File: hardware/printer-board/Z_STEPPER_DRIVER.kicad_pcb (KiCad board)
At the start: 2 copper layers, 7 parts, among them J7 MS_SELECT, J8 TO_MOTOR, U5 A4988_MODULE

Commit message: update heater layouts,
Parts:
- removed C11: CP100uf,25V, Capacitor_SMD:CP_Elec_6.3x7.7
- removed R9: R103,0603, Resistor_SMD:R_0603_1608Metric_Pad1.05x0.95mm_HandSolder
- added C9: C104,0603, Capacitor_SMD:C_0603_1608Metric_Pad1.05x0.95mm_HandSolder, F.Cu at (38.0, 31.5)
- added D22: LED_BLUE,0603, LED_SMD:LED_0603_1608Metric_Pad1.05x0.95mm_HandSolder, F.Cu at (43.5, 53.0)
- added R15: R102,0603, Resistor_SMD:R_0603_1608Metric_Pad1.05x0.95mm_HandSolder, B.Cu at (43.5, 53.0)
- added R19: R103,0603, Resistor_SMD:R_0603_1608Metric_Pad1.05x0.95mm_HandSolder, F.Cu at (41.5, 33.5)
- J8: value TO_MOTOR -> Z
- moved J8 22.4 mm to (32.5, 53.0), turned to 90 degrees
- moved R8 10.1 mm to (41.5, 37.5)
- moved J7 1.58 mm to (35.5, 35.5)
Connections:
- net +5V renamed +3V3_STM32
- net /DIR renamed /Z_DIR
- net /STEP renamed /Z_STEP
- U5 pad 1: /~EN~ -> /~Z_EN~
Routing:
- net +3V3_STM32: track 33.6 -> 0.00 mm
- net GND: track 31.9 -> 0.00 mm
- net +12V: track 19.8 -> 0.00 mm
- net Net-(J7-Pad1): track 16.6 -> 0.00 mm
- net Net-(J7-Pad5): track 5.82 -> 0.00 mm
- net Net-(J7-Pad3): track 5.82 -> 0.00 mm
- net Net-(J8-Pad4): track 3.41 -> 0.00 mm
- net Net-(J8-Pad3): track 3.41 -> 0.00 mm
- net Net-(J8-Pad2): track 3.41 -> 0.00 mm
- net Net-(J8-Pad1): track 3.41 -> 0.00 mm
- net /~EN~: track 3.40 -> 0.00 mm
- net Net-(U5-Pad5): track 2.54 -> 0.00 mm

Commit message: update,
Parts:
- J8: footprint Connector_PinHeader_2.54mm:PinHeader_1x04_P2.54mm_Vertical -> footprint-lib:b4b-ph-kl,stepper_terminal
- U5: footprint Module:Pololu_Breakout-16_15.2x20.3mm -> footprint-lib:Pololu_Breakout-16_15.2x20.3mm
- moved J8 3.71 mm to (36.2, 53.2), turned to 0 degrees

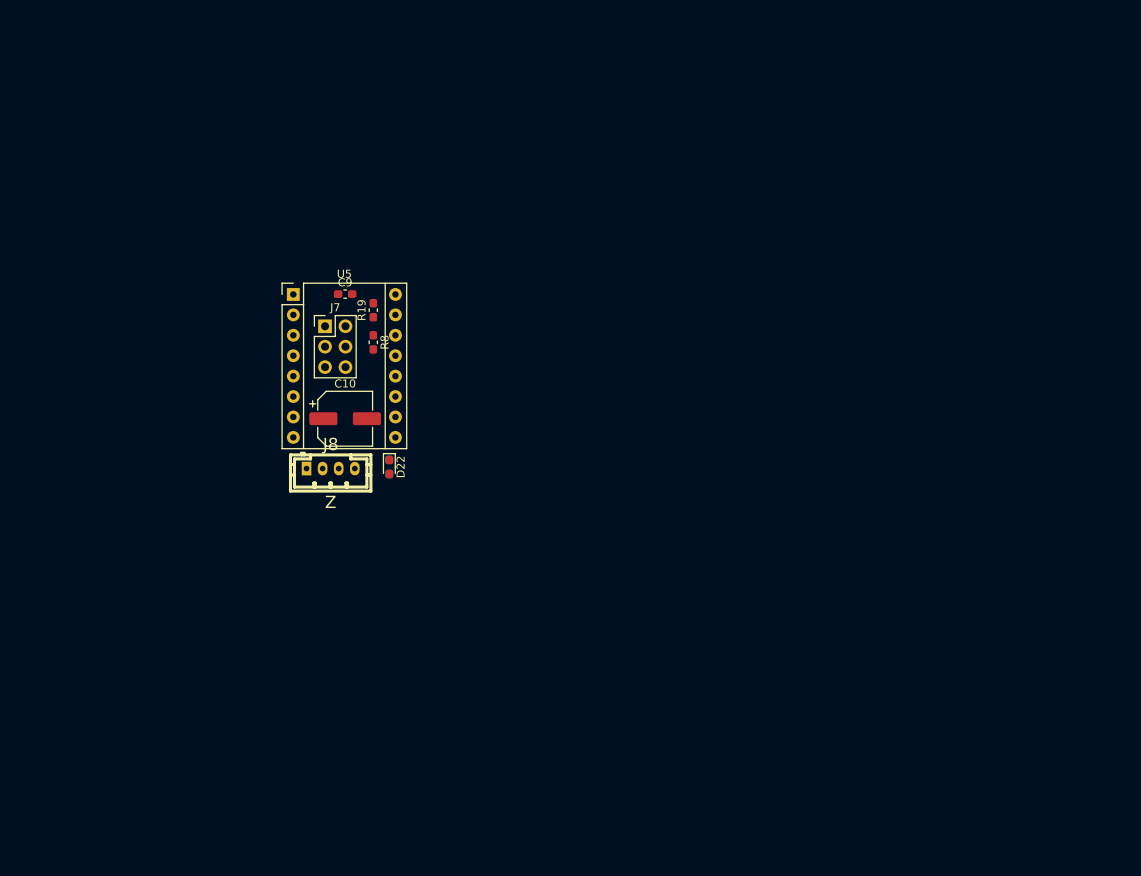
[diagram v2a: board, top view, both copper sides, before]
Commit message: update for stepper Z,
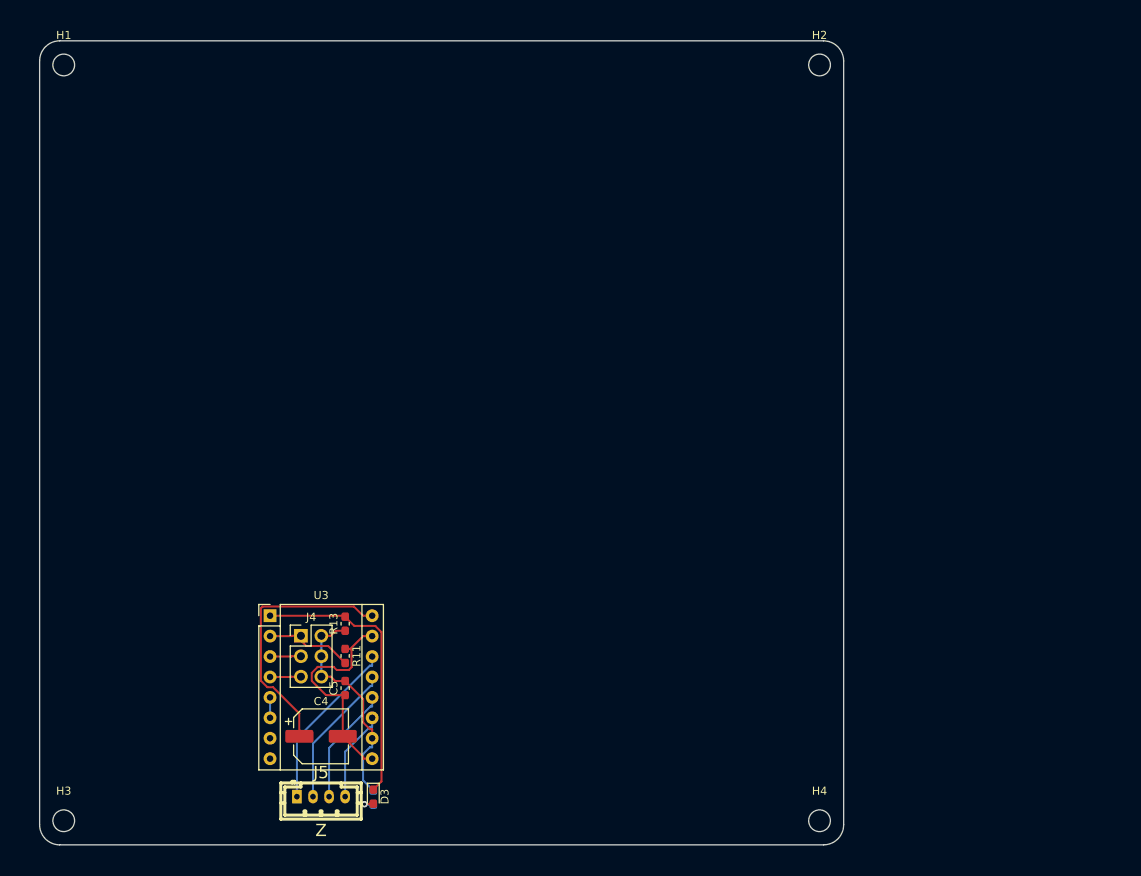
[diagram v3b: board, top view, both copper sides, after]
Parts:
- removed C10: CP100uf,25V, Capacitor_SMD:CP_Elec_6.3x7.7
- removed C9: C104,0603, Capacitor_SMD:C_0603_1608Metric_Pad1.05x0.95mm_HandSolder
- removed D22: LED_BLUE,0603, LED_SMD:LED_0603_1608Metric_Pad1.05x0.95mm_HandSolder
- removed J7: MS_SELECT, Connector_PinHeader_2.54mm:PinHeader_2x03_P2.54mm_Vertical
- removed J8: Z, footprint-lib:b4b-ph-kl,stepper_terminal
- removed R15: R102,0603, Resistor_SMD:R_0603_1608Metric_Pad1.05x0.95mm_HandSolder
- removed R19: R103,0603, Resistor_SMD:R_0603_1608Metric_Pad1.05x0.95mm_HandSolder
- removed R8: R104,0603, Resistor_SMD:R_0603_1608Metric_Pad1.05x0.95mm_HandSolder
- removed U5: A4988_MODULE, footprint-lib:Pololu_Breakout-16_15.2x20.3mm
- added C4: CP100uf,25V, Capacitor_SMD:CP_Elec_6.3x7.7, F.Cu at (35.0, 86.5)
- added C5: C104,0603, Capacitor_SMD:C_0603_1608Metric_Pad1.05x0.95mm_HandSolder, F.Cu at (38.0, 80.5)
- added D3: LED_BLUE,0603, LED_SMD:LED_0603_1608Metric_Pad1.05x0.95mm_HandSolder, F.Cu at (41.5, 94.0)
- added H1: MOUNT_M3, MountingHole:MountingHole_2.7mm_M2.5, F.Cu at (3.00, 3.00)
- added H2: MOUNT_M3, MountingHole:MountingHole_2.7mm_M2.5, F.Cu at (97.0, 3.00)
- added H3: MOUNT_M3, MountingHole:MountingHole_2.7mm_M2.5, F.Cu at (3.00, 97.0)
- added H4: MOUNT_M3, MountingHole:MountingHole_2.7mm_M2.5, F.Cu at (97.0, 97.0)
- added J4: MS_SELECT, Connector_PinHeader_2.54mm:PinHeader_2x03_P2.54mm_Vertical, F.Cu at (32.5, 74.0)
- added J5: Z, footprint-lib:b4b-ph-kl,stepper_terminal, F.Cu at (35.0, 94.0)
- added R11: R104,0603, Resistor_SMD:R_0603_1608Metric_Pad1.05x0.95mm_HandSolder, F.Cu at (38.0, 76.5)
- added R12: R102,0603, Resistor_SMD:R_0603_1608Metric_Pad1.05x0.95mm_HandSolder, B.Cu at (41.5, 94.1)
- added R13: R103,0603, Resistor_SMD:R_0603_1608Metric_Pad1.05x0.95mm_HandSolder, F.Cu at (38.0, 72.5)
- added U3: A4988_MODULE, footprint-lib:Pololu_Breakout-16_15.2x20.3mm, F.Cu at (28.7, 71.5)
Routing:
- net /Z_~E1_STEP~PER_DRIVER/~Z_EN~: track 0.00 -> 34.7 mm
- net +12V: track 0.00 -> 32.7 mm
- net GND: track 0.00 -> 27.9 mm
- net +3V3: track 0.00 -> 27.8 mm
- net Net-(J5-Pad1): track 0.00 -> 21.5 mm
- net Net-(J5-Pad2): track 0.00 -> 18.0 mm
- net Net-(J5-Pad3): track 0.00 -> 14.7 mm
- net Net-(J5-Pad4): track 0.00 -> 11.4 mm
- net Net-(J4-Pad1): track 0.00 -> 11.3 mm
- net Net-(J4-Pad5): track 0.00 -> 3.86 mm
- net Net-(J4-Pad3): track 0.00 -> 3.86 mm
- net Net-(U3-Pad5): track 0.00 -> 2.54 mm
- net Net-(D3-Pad2): track 0.00 -> 2.25 mm, vias 0 -> 1
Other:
- board outline added: 100 x 100 mm

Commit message: update,
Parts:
- removed H1, H2, H3, H4: MOUNT_M3, MountingHole:MountingHole_2.7mm_M2.5
- moved C4 73.1 mm to (9.50, 18.0)
- moved C5 73.1 mm to (12.5, 12.0)
- moved D3 73.1 mm to (16.0, 25.5)
- moved J4 73.1 mm to (7.00, 5.50)
- moved J5 73.1 mm to (9.50, 25.5)
- moved R11 73.1 mm to (12.5, 8.00)
- moved R12 73.1 mm to (16.0, 25.6)
- moved R13 73.1 mm to (12.5, 4.00)
- moved U3 73.1 mm to (3.16, 3.00)
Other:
- board outline removed

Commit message: update,
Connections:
- net +3V3 renamed +3V3_STM32
- net /Z_~E1_STEP~PER_DRIVER/Z_DIR renamed /Z_DIR
- net /Z_~E1_STEP~PER_DRIVER/Z_STEP renamed /Z_STEP
- net /Z_~E1_STEP~PER_DRIVER/~Z_EN~ renamed /~Z_EN~

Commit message: update,
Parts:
- added C1: CP100uf,10V, Capacitor_SMD:CP_Elec_6.3x5.3, F.Cu at (76.3, 33.4)
- added C10: CP100uf,25V, Capacitor_SMD:CP_Elec_6.3x7.7, F.Cu at (9.23, 64.2)
- added C11: C104,0603, Capacitor_SMD:C_0603_1608Metric_Pad1.05x0.95mm_HandSolder, F.Cu at (20.6, 67.2)
- added C12: CP100uf,25V, Capacitor_SMD:CP_Elec_6.3x7.7, F.Cu at (9.23, 48.3)
- added C13: C104,0603, Capacitor_SMD:C_0603_1608Metric_Pad1.05x0.95mm_HandSolder, F.Cu at (16.8, 51.3)
- added C14: C106,0603, Capacitor_SMD:C_0603_1608Metric_Pad1.05x0.95mm_HandSolder, B.Cu at (2.75, 31.8)
- added C15: C106,0603, Capacitor_SMD:C_0603_1608Metric_Pad1.05x0.95mm_HandSolder, B.Cu at (10.0, 31.8)
- added C16: C106,0603, Capacitor_SMD:C_0603_1608Metric_Pad1.05x0.95mm_HandSolder, B.Cu at (16.8, 31.8)
- added C17: C106,0603, Capacitor_SMD:C_0603_1608Metric_Pad1.05x0.95mm_HandSolder, B.Cu at (23.5, 31.8)
- added C18: C106,0603, Capacitor_SMD:C_0603_1608Metric_Pad1.05x0.95mm_HandSolder, B.Cu at (27.4, 20.1)
- added C19: C104,0603, Capacitor_SMD:C_0603_1608Metric_Pad1.05x0.95mm_HandSolder, F.Cu at (11.0, 1.75)
- added C2: CP100uf,25V, Capacitor_SMD:CP_Elec_6.3x7.7, F.Cu at (90.5, 90.2)
- added C20: CP100uf,35V, Capacitor_SMD:CP_Elec_6.3x7.7, F.Cu at (11.8, 9.35)
- added C21: C104,0603, Capacitor_SMD:C_0603_1608Metric_Pad1.05x0.95mm_HandSolder, B.Cu at (40.2, 69.8)
- added C22: C10pf,0603, Capacitor_SMD:C_0603_1608Metric_Pad1.05x0.95mm_HandSolder, B.Cu at (28.5, 62.2)
- added C23: C104,0603, Capacitor_SMD:C_0603_1608Metric_Pad1.05x0.95mm_HandSolder, B.Cu at (33.1, 60.3)
- added C24: C10pf,0603, Capacitor_SMD:C_0603_1608Metric_Pad1.05x0.95mm_HandSolder, B.Cu at (35.8, 69.2)
- added C25: C104,0603, Capacitor_SMD:C_0603_1608Metric_Pad1.05x0.95mm_HandSolder, B.Cu at (31.4, 56.1)
- added C26: C104,0603, Capacitor_SMD:C_0603_1608Metric_Pad1.05x0.95mm_HandSolder, B.Cu at (42.3, 47.9)
- added C27: C104,0603, Capacitor_SMD:C_0603_1608Metric_Pad1.05x0.95mm_HandSolder, B.Cu at (50.8, 58.5)
- added C28: C104,0603, Capacitor_SMD:C_0603_1608Metric_Pad1.05x0.95mm_HandSolder, B.Cu at (42.6, 66.6)
- added C29: C105,0603, Capacitor_SMD:C_0603_1608Metric_Pad1.05x0.95mm_HandSolder, B.Cu at (34.7, 61.9)
- added C3: C104,0603, Capacitor_SMD:C_0603_1608Metric_Pad1.05x0.95mm_HandSolder, F.Cu at (93.5, 74.8)
- added C30: C104,0603, Capacitor_SMD:C_0603_1608Metric_Pad1.05x0.95mm_HandSolder, B.Cu at (49.7, 59.6)
- added C31: C104,0603, Capacitor_SMD:C_0603_1608Metric_Pad1.05x0.95mm_HandSolder, B.Cu at (43.3, 49.0)
- added C32: C104,0603, Capacitor_SMD:C_0603_1608Metric_Pad1.05x0.95mm_HandSolder, B.Cu at (47.6, 68.0)
- added C36: CP1uf,50V, Capacitor_SMD:CP_Elec_4x5.3, F.Cu at (21.5, 13.8)
- added C37: CP1uf,50V, Capacitor_SMD:CP_Elec_4x5.3, F.Cu at (29.5, 13.8)
- added C38: CP1uf,50V, Capacitor_SMD:CP_Elec_4x5.3, F.Cu at (38.0, 13.8)
- added C39: CP100uf,25V, Capacitor_SMD:CP_Elec_6.3x7.7, F.Cu at (25.7, 90.2)
- added C40: C104,0603, Capacitor_SMD:C_0603_1608Metric_Pad1.05x0.95mm_HandSolder, F.Cu at (29.8, 78.6)
- added C41: CP100uf,25V, Capacitor_SMD:CP_Elec_6.3x7.7, F.Cu at (74.3, 90.2)
- added C42: C104,0603, Capacitor_SMD:C_0603_1608Metric_Pad1.05x0.95mm_HandSolder, F.Cu at (77.8, 74.8)
- added C43: C104,0603, Capacitor_SMD:C_0603_1608Metric_Pad1.05x0.95mm_HandSolder, F.Cu at (133.3, 61.4)
- added C44: CP100uf,16V, Capacitor_SMD:CP_Elec_6.3x5.3, F.Cu at (37.2, 21.0)
- added C45: C106,0603, Capacitor_SMD:C_0603_1608Metric_Pad1.05x0.95mm_HandSolder, F.Cu at (67.5, 33.5)
- added C46: C104,0603, Capacitor_SMD:C_0603_1608Metric_Pad1.05x0.95mm_HandSolder, F.Cu at (71.5, 40.0)
- added C47: C332,0603, Capacitor_SMD:C_0603_1608Metric_Pad1.05x0.95mm_HandSolder, F.Cu at (63.0, 41.0)
- added C48: C103,0603, Capacitor_SMD:C_0603_1608Metric_Pad1.05x0.95mm_HandSolder, F.Cu at (70.0, 32.5)
- added C49: C226,6.3v,0603, Capacitor_SMD:C_0603_1608Metric_Pad1.05x0.95mm_HandSolder, F.Cu at (63.0, 37.5)
- added C50: C106,0603, Capacitor_SMD:C_0603_1608Metric_Pad1.05x0.95mm_HandSolder, F.Cu at (48.2, 40.2)
- added C51: C104,0603, Capacitor_SMD:C_0603_1608Metric_Pad1.05x0.95mm_HandSolder, F.Cu at (43.5, 33.2)
- added C52: C332,0603, Capacitor_SMD:C_0603_1608Metric_Pad1.05x0.95mm_HandSolder, F.Cu at (49.2, 30.0)
- added C53: C103,0603, Capacitor_SMD:C_0603_1608Metric_Pad1.05x0.95mm_HandSolder, F.Cu at (45.5, 40.8)
- added C54: C226,6.3v,0603, Capacitor_SMD:C_0603_1608Metric_Pad1.05x0.95mm_HandSolder, F.Cu at (52.3, 35.5)
- added C55: C105,0603, Capacitor_SMD:C_0603_1608Metric_Pad1.05x0.95mm_HandSolder, B.Cu at (38.7, 65.9)
- added C6: CP100uf,25V, Capacitor_SMD:CP_Elec_6.3x7.7, F.Cu at (41.9, 90.2)
- added C7: C104,0603, Capacitor_SMD:C_0603_1608Metric_Pad1.05x0.95mm_HandSolder, F.Cu at (45.8, 78.6)
- added C8: CP100uf,25V, Capacitor_SMD:CP_Elec_6.3x7.7, F.Cu at (9.50, 90.2)
- added C9: C104,0603, Capacitor_SMD:C_0603_1608Metric_Pad1.05x0.95mm_HandSolder, F.Cu at (12.5, 82.5)
- added D1: 5V HEALTHY, LED_SMD:LED_0603_1608Metric_Pad1.05x0.95mm_HandSolder, F.Cu at (50.8, 70.8)
- added D10: LED_BLUE,0603, LED_SMD:LED_0603_1608Metric_Pad1.05x0.95mm_HandSolder, F.Cu at (91.9, 9.25)
- added D11: LED_BLUE,0603, LED_SMD:LED_0603_1608Metric_Pad1.05x0.95mm_HandSolder, F.Cu at (93.7, 9.30)
- added D12: LED_BLUE,0603, LED_SMD:LED_0603_1608Metric_Pad1.05x0.95mm_HandSolder, F.Cu at (95.4, 9.30)
- added D13: LED_BLUE,0603, LED_SMD:LED_0603_1608Metric_Pad1.05x0.95mm_HandSolder, F.Cu at (98.9, 9.30)
- added D14: LED_BLUE,0603, LED_SMD:LED_0603_1608Metric_Pad1.05x0.95mm_HandSolder, F.Cu at (97.2, 9.30)
- added D15: SD_M4, Diode_SMD:D_SOD-323_HandSoldering, F.Cu at (11.2, 3.75)
- added D16: SD_M4, Diode_SMD:D_SOD-323_HandSoldering, F.Cu at (21.4, 21.4)
- added D17: PB9, LED_SMD:LED_0603_1608Metric_Pad1.05x0.95mm_HandSolder, F.Cu at (30.3, 52.5)
- added D18: LED_RED,0603, LED_SMD:LED_0603_1608Metric_Pad1.05x0.95mm_HandSolder, F.Cu at (63.9, 5.50)
- added D19: LED_RED,0603, LED_SMD:LED_0603_1608Metric_Pad1.05x0.95mm_HandSolder, F.Cu at (75.8, 5.50)
- added D2: LED_BLUE,0603, LED_SMD:LED_0603_1608Metric_Pad1.05x0.95mm_HandSolder, F.Cu at (92.2, 97.7)
- added D20: LED_BLUE,0603, LED_SMD:LED_0603_1608Metric_Pad1.05x0.95mm_HandSolder, F.Cu at (25.1, 2.52)
- added D21: LED_BLUE,0603, LED_SMD:LED_0603_1608Metric_Pad1.05x0.95mm_HandSolder, F.Cu at (33.4, 2.52)
- added D22: LED_BLUE,0603, LED_SMD:LED_0603_1608Metric_Pad1.05x0.95mm_HandSolder, F.Cu at (41.8, 2.50)
- added D23: LED_BLUE,0603, LED_SMD:LED_0603_1608Metric_Pad1.05x0.95mm_HandSolder, F.Cu at (33.0, 97.7)
- added D24: LED_BLUE,0603, LED_SMD:LED_0603_1608Metric_Pad1.05x0.95mm_HandSolder, F.Cu at (78.2, 97.7)
- added D4: LED_BLUE,0603, LED_SMD:LED_0603_1608Metric_Pad1.05x0.95mm_HandSolder, F.Cu at (48.1, 97.7)
- added D5: LED_BLUE,0603, LED_SMD:LED_0603_1608Metric_Pad1.05x0.95mm_HandSolder, F.Cu at (17.8, 97.7)
- added D6: LED_BLUE,0603, LED_SMD:LED_0603_1608Metric_Pad1.05x0.95mm_HandSolder, F.Cu at (3.00, 70.5)
- added D7: LED_BLUE,0603, LED_SMD:LED_0603_1608Metric_Pad1.05x0.95mm_HandSolder, F.Cu at (3.00, 54.7)
- added D8: LED_RED,0603, LED_SMD:LED_0603_1608Metric_Pad1.05x0.95mm_HandSolder, F.Cu at (51.8, 5.50)
- added D9: LED_BLUE,0603, LED_SMD:LED_0603_1608Metric_Pad1.05x0.95mm_HandSolder, F.Cu at (90.2, 9.25)
- added F1: 16V/30A, w_misc_comp:fuse_smf, F.Cu at (11.8, 17.9)
- added F2: 30V/5A, w_misc_comp:fuse_smf, F.Cu at (11.8, 26.4)
- added H1: MOUNT_M3, MountingHole:MountingHole_2.7mm_M2.5, F.Cu at (3.00, 3.00)
- added H2: MOUNT_M3, MountingHole:MountingHole_2.7mm_M2.5, F.Cu at (97.0, 3.00)
- added H3: MOUNT_M3, MountingHole:MountingHole_2.7mm_M2.5, F.Cu at (3.00, 97.0)
- added H4: MOUNT_M3, MountingHole:MountingHole_2.7mm_M2.5, F.Cu at (97.0, 97.0)
- added J1: USB_DEBUG, Connector_PinHeader_1.27mm:PinHeader_1x05_P1.27mm_Vertical, F.Cu at (91.4, 65.4)
- added J10: MS_SELECT, Connector_PinHeader_2.54mm:PinHeader_2x03_P2.54mm_Vertical, F.Cu at (22.5, 61.2)
- added J11: E0, footprint-lib:b4b-ph-kl,stepper_terminal, F.Cu at (2.40, 64.2)
- added J12: MS_SELECT, Connector_PinHeader_2.54mm:PinHeader_2x03_P2.54mm_Vertical, F.Cu at (22.4, 45.3)
- added J13: E1, footprint-lib:b4b-ph-kl,stepper_terminal, F.Cu at (2.40, 48.2)
- added J14: HEATBED, footprint-lib:mpt_0,5%2f2-2,54,heatbed, F.Cu at (46.8, 3.00)
- added J15: X_MIN, footprint-lib:b3b-ph-kl,end_stop, F.Cu at (85.0, 2.25)
- added J16: X_MAX, footprint-lib:b3b-ph-kl,end_stop, F.Cu at (85.0, 8.00)
- added J17: Y_MIN, footprint-lib:b3b-ph-kl,end_stop, F.Cu at (85.0, 13.8)
- added J18: Y_MAX, footprint-lib:b3b-ph-kl,end_stop, F.Cu at (85.0, 19.5)
- added J19: Z_MIN, footprint-lib:b3b-ph-kl,end_stop, F.Cu at (94.5, 13.5)
- added J2: MS_SELECT, Connector_PinHeader_2.54mm:PinHeader_2x03_P2.54mm_Vertical, F.Cu at (87.5, 77.0)
- added J20: Z_MAX, footprint-lib:b3b-ph-kl,end_stop, F.Cu at (94.5, 19.5)
- added J21: HEATBED_TEMP, w_conn_jst-ph:b2b-ph-kl, F.Cu at (2.39, 36.2)
- added J22: HOTEND_TEMP0, w_conn_jst-ph:b2b-ph-kl, F.Cu at (9.26, 36.2)
- added J23: HOTEND_TEMP1, w_conn_jst-ph:b2b-ph-kl, F.Cu at (16.1, 36.2)
- added J24: AUX_TEMP, w_conn_jst-ph:b2b-ph-kl, F.Cu at (23.0, 36.2)
- added J25: 12V_INPUT_2, footprint-lib:mpt_0,5%2f2-2,54,12V_SRC, F.Cu at (3.25, 18.2)
- added J26: 12V_INPUT, footprint-lib:mpt_0,5%2f2-2,54,12V_SRC, F.Cu at (3.15, 26.4)
- added J27: 12V_OUT, footprint-lib:mpt_0,5%2f2-2,54,12V_SRC, F.Cu at (3.15, 10.2)
- added J28: SWD, Connector_PinHeader_1.27mm:PinHeader_1x04_P1.27mm_Vertical, F.Cu at (37.4, 42.6)
- added J29: USB_DEBUG, Connector_PinHeader_1.27mm:PinHeader_1x05_P1.27mm_Vertical, F.Cu at (33.4, 47.6)
- added J3: X, footprint-lib:b4b-ph-kl,stepper_terminal, F.Cu at (86.0, 97.3)
- added J30: PWR_DEBUG, Connector_PinHeader_1.27mm:PinHeader_1x05_P1.27mm_Vertical, F.Cu at (29.4, 42.8)
- added J31: HOT_END, footprint-lib:mpt_0,5%2f2-2,54,heatbed, F.Cu at (58.8, 3.00)
- added J32: HOT_END, footprint-lib:mpt_0,5%2f2-2,54,heatbed, F.Cu at (70.8, 3.00)
- added J33: TO FAN0, footprint-lib:b2b-ph-kl,fan_pwm_out, F.Cu at (21.0, 2.00)
- added J34: TO FAN1, footprint-lib:b2b-ph-kl,fan_pwm_out, F.Cu at (29.2, 2.00)
- added J35: TO FAN2, footprint-lib:b2b-ph-kl,fan_pwm_out, F.Cu at (37.5, 2.00)
- added J36: MS_SELECT, Connector_PinHeader_2.54mm:PinHeader_2x03_P2.54mm_Vertical, F.Cu at (22.7, 77.0)
- added J37: Z2, footprint-lib:b4b-ph-kl,stepper_terminal, F.Cu at (26.7, 97.3)
- added J38: MS_SELECT, Connector_PinHeader_2.54mm:PinHeader_2x03_P2.54mm_Vertical, F.Cu at (71.3, 77.0)
- added J39: Y, footprint-lib:b4b-ph-kl,stepper_terminal, F.Cu at (71.9, 97.3)
- added J40: Conn_01x07, Connector_PinHeader_1.27mm:PinHeader_1x07_P1.27mm_Vertical, F.Cu at (124.0, 61.8)
- added J41: EXP1, Connector_PinHeader_2.54mm:PinHeader_2x05_P2.54mm_Vertical, F.Cu at (39.0, 38.4)
- added J42: EXP2, Connector_PinHeader_2.54mm:PinHeader_2x05_P2.54mm_Vertical, F.Cu at (31.8, 38.4)
- added J6: MS_SELECT, Connector_PinHeader_2.54mm:PinHeader_2x03_P2.54mm_Vertical, F.Cu at (38.9, 77.0)
- added J7: Z1, footprint-lib:b4b-ph-kl,stepper_terminal, F.Cu at (41.8, 97.3)
- added J8: MS_SELECT, Connector_PinHeader_2.54mm:PinHeader_2x03_P2.54mm_Vertical, F.Cu at (6.50, 77.0)
- added J9: Z3, footprint-lib:b4b-ph-kl,stepper_terminal, F.Cu at (11.6, 97.3)
- added JP5: Jumper_NO_Small, SolderJumper-2_P1.3mm_Open_TrianglePad1.0x1.5mm, B.Cu at (8.55, 22.2)
- added JP6: Jumper_NO_Small, SolderJumper-2_P1.3mm_Open_TrianglePad1.0x1.5mm, B.Cu at (42.3, 58.2)
- added JP7: Jumper_NO_Small, SolderJumper-2_P1.3mm_Open_TrianglePad1.0x1.5mm, B.Cu at (44.2, 60.1)
- added JP8: SolderJumper_3_Open, Jumper:SolderJumper-3_P2.0mm_Open_TrianglePad1.0x1.5mm_NumberLabels, F.Cu at (128.6, 61.9)
- added L1: L_Small, w_smd_inductors:inductor_smd_0603, F.Cu at (40.2, 69.8)
- added L2: L_15uH, w_smd_inductors:inductor_smd_4.8x2.8mm, F.Cu at (61.8, 33.8)
- added L3: L_15uH, w_smd_inductors:inductor_smd_4.8x2.8mm, F.Cu at (53.5, 39.2)
- added Q1: WSK220N04, footprint-lib:TO-263-2,thermal_vias, F.Cu at (49.2, 15.0)
- added Q2: STP55NF06, footprint-lib:TO-263-2,thermal_vias, F.Cu at (61.2, 15.0)
- added Q3: STP55NF06, footprint-lib:TO-263-2,thermal_vias, F.Cu at (73.2, 15.0)
- added Q4: D882, footprint-lib:SOT-89-3,thermal_vias, F.Cu at (21.1, 8.00)
- added Q5: D882, footprint-lib:SOT-89-3,thermal_vias, F.Cu at (29.2, 8.00)
- added Q6: D882, footprint-lib:SOT-89-3,thermal_vias, F.Cu at (37.8, 8.00)
- added R1: R153,0603, Resistor_SMD:R_0603_1608Metric_Pad1.05x0.95mm_HandSolder, F.Cu at (76.2, 61.5)
- added R10: R103,0603, Resistor_SMD:R_0603_1608Metric_Pad1.05x0.95mm_HandSolder, F.Cu at (93.5, 82.5)
- added R14: R104,0603, Resistor_SMD:R_0603_1608Metric_Pad1.05x0.95mm_HandSolder, F.Cu at (45.8, 74.8)
- added R15: R102,0603, Resistor_SMD:R_0603_1608Metric_Pad1.05x0.95mm_HandSolder, B.Cu at (48.0, 97.7)
- added R16: R103,0603, Resistor_SMD:R_0603_1608Metric_Pad1.05x0.95mm_HandSolder, F.Cu at (45.8, 82.5)
- added R17: R104,0603, Resistor_SMD:R_0603_1608Metric_Pad1.05x0.95mm_HandSolder, F.Cu at (12.5, 78.6)
- added R18: R102,0603, Resistor_SMD:R_0603_1608Metric_Pad1.05x0.95mm_HandSolder, B.Cu at (17.8, 97.7)
- added R19: R103,0603, Resistor_SMD:R_0603_1608Metric_Pad1.05x0.95mm_HandSolder, F.Cu at (12.5, 74.8)
- added R2: R153,0603, Resistor_SMD:R_0603_1608Metric_Pad1.05x0.95mm_HandSolder, F.Cu at (78.2, 61.5)
- added R20: R104,0603, Resistor_SMD:R_0603_1608Metric_Pad1.05x0.95mm_HandSolder, F.Cu at (24.4, 67.2)
- added R21: R102,0603, Resistor_SMD:R_0603_1608Metric_Pad1.05x0.95mm_HandSolder, B.Cu at (3.00, 70.5)
- added R22: R103,0603, Resistor_SMD:R_0603_1608Metric_Pad1.05x0.95mm_HandSolder, F.Cu at (16.8, 67.2)
- added R23: R104,0603, Resistor_SMD:R_0603_1608Metric_Pad1.05x0.95mm_HandSolder, F.Cu at (20.6, 51.3)
- added R24: R102,0603, Resistor_SMD:R_0603_1608Metric_Pad1.05x0.95mm_HandSolder, F.Cu at (24.4, 51.3)
- added R25: R103,0603, Resistor_SMD:R_0603_1608Metric_Pad1.05x0.95mm_HandSolder, B.Cu at (3.00, 54.7)
- added R26: R100,0805, Resistor_SMD:R_0805_2012Metric_Pad1.15x1.40mm_HandSolder, B.Cu at (46.8, 19.5)
- added R27: R104,0805, Resistor_SMD:R_0805_2012Metric_Pad1.15x1.40mm_HandSolder, B.Cu at (51.8, 19.5)
- added R28: R182,0603, Resistor_SMD:R_0603_1608Metric_Pad1.05x0.95mm_HandSolder, B.Cu at (51.8, 5.50)
- added R29: R102,0603, Resistor_SMD:R_0603_1608Metric_Pad1.05x0.95mm_HandSolder, B.Cu at (90.2, 9.25)
- added R30: R102,0603, Resistor_SMD:R_0603_1608Metric_Pad1.05x0.95mm_HandSolder, B.Cu at (91.9, 9.25)
- added R31: R102,0603, Resistor_SMD:R_0603_1608Metric_Pad1.05x0.95mm_HandSolder, B.Cu at (93.7, 9.30)
- added R32: R102,0603, Resistor_SMD:R_0603_1608Metric_Pad1.05x0.95mm_HandSolder, B.Cu at (95.4, 9.30)
- added R33: R102,0603, Resistor_SMD:R_0603_1608Metric_Pad1.05x0.95mm_HandSolder, B.Cu at (98.9, 9.30)
- added R34: R102,0603, Resistor_SMD:R_0603_1608Metric_Pad1.05x0.95mm_HandSolder, B.Cu at (97.2, 9.30)
- added R35: R472,0603, Resistor_SMD:R_0603_1608Metric_Pad1.05x0.95mm_HandSolder, F.Cu at (2.75, 31.8)
- added R36: R472,0603, Resistor_SMD:R_0603_1608Metric_Pad1.05x0.95mm_HandSolder, F.Cu at (10.0, 31.8)
- added R37: R472,0603, Resistor_SMD:R_0603_1608Metric_Pad1.05x0.95mm_HandSolder, F.Cu at (16.8, 31.8)
- added R38: R472,0603, Resistor_SMD:R_0603_1608Metric_Pad1.05x0.95mm_HandSolder, F.Cu at (23.5, 31.8)
- added R39: R472,0603, Resistor_SMD:R_0603_1608Metric_Pad1.05x0.95mm_HandSolder, F.Cu at (27.4, 20.1)
- added R4: R220,0603, Resistor_SMD:R_0603_1608Metric_Pad1.05x0.95mm_HandSolder, B.Cu at (86.1, 70.8)
- added R40: R472,0603, Resistor_SMD:R_0603_1608Metric_Pad1.05x0.95mm_HandSolder, B.Cu at (44.6, 55.9)
- added R41: R472,0603, Resistor_SMD:R_0603_1608Metric_Pad1.05x0.95mm_HandSolder, B.Cu at (46.5, 57.8)
- added R42: R0,0603, Resistor_SMD:R_0603_1608Metric_Pad1.05x0.95mm_HandSolder, B.Cu at (37.7, 64.9)
- added R43: R0,0603, Resistor_SMD:R_0603_1608Metric_Pad1.05x0.95mm_HandSolder, B.Cu at (36.6, 63.8)
- added R44: R102,0603, Resistor_SMD:R_0603_1608Metric_Pad1.05x0.95mm_HandSolder, B.Cu at (30.3, 52.5)
- added R45: R103,0603, Resistor_SMD:R_0603_1608Metric_Pad1.05x0.95mm_HandSolder, B.Cu at (40.2, 56.0)
- added R46: R103,0603, Resistor_SMD:R_0603_1608Metric_Pad1.05x0.95mm_HandSolder, B.Cu at (39.1, 55.0)
- added R47: R220,0603, Resistor_SMD:R_0603_1608Metric_Pad1.05x0.95mm_HandSolder, F.Cu at (51.5, 50.2)
- added R48: R220,0603, Resistor_SMD:R_0603_1608Metric_Pad1.05x0.95mm_HandSolder, F.Cu at (51.5, 51.8)
- added R49: R152,0603, Resistor_SMD:R_0603_1608Metric_Pad1.05x0.95mm_HandSolder, B.Cu at (51.6, 51.0)
- added R5: R220,0603, Resistor_SMD:R_0603_1608Metric_Pad1.05x0.95mm_HandSolder, B.Cu at (84.5, 70.8)
- added R50: R100,0805, Resistor_SMD:R_0805_2012Metric_Pad1.15x1.40mm_HandSolder, B.Cu at (58.8, 19.5)
- added R51: R104,0805, Resistor_SMD:R_0805_2012Metric_Pad1.15x1.40mm_HandSolder, B.Cu at (63.8, 19.5)
- added R52: R182,0603, Resistor_SMD:R_0603_1608Metric_Pad1.05x0.95mm_HandSolder, B.Cu at (63.8, 5.50)
- added R53: R100,0805, Resistor_SMD:R_0805_2012Metric_Pad1.15x1.40mm_HandSolder, B.Cu at (70.8, 20.0)
- added R54: R104,0805, Resistor_SMD:R_0805_2012Metric_Pad1.15x1.40mm_HandSolder, B.Cu at (75.8, 20.0)
- added R55: R182,0603, Resistor_SMD:R_0603_1608Metric_Pad1.05x0.95mm_HandSolder, B.Cu at (75.8, 5.50)
- added R56: R100,0805, Resistor_SMD:R_0805_2012Metric_Pad1.15x1.40mm_HandSolder, B.Cu at (22.9, 5.10)
- added R57: R104,0805, Resistor_SMD:R_0805_2012Metric_Pad1.15x1.40mm_HandSolder, B.Cu at (19.4, 5.10)
- added R58: R100,0603, Resistor_SMD:R_0603_1608Metric_Pad1.05x0.95mm_HandSolder, B.Cu at (25.1, 2.50)
- added R59: R182,0603, Resistor_SMD:R_0603_1608Metric_Pad1.05x0.95mm_HandSolder, B.Cu at (21.1, 5.10)
- added R6: R152,0603, Resistor_SMD:R_0603_1608Metric_Pad1.05x0.95mm_HandSolder, B.Cu at (82.9, 70.8)
- added R60: R100,0805, Resistor_SMD:R_0805_2012Metric_Pad1.15x1.40mm_HandSolder, B.Cu at (31.0, 5.25)
- added R61: R104,0805, Resistor_SMD:R_0805_2012Metric_Pad1.15x1.40mm_HandSolder, B.Cu at (27.5, 5.25)
- added R62: R100,0603, Resistor_SMD:R_0603_1608Metric_Pad1.05x0.95mm_HandSolder, B.Cu at (29.2, 5.38)
- added R63: R182,0603, Resistor_SMD:R_0603_1608Metric_Pad1.05x0.95mm_HandSolder, B.Cu at (33.4, 2.50)
- added R64: R100,0805, Resistor_SMD:R_0603_1608Metric_Pad1.05x0.95mm_HandSolder, B.Cu at (39.2, 5.25)
- added R65: R104,0805, Resistor_SMD:R_0805_2012Metric_Pad1.15x1.40mm_HandSolder, B.Cu at (36.0, 5.25)
- added R66: R100,0603, Resistor_SMD:R_0603_1608Metric_Pad1.05x0.95mm_HandSolder, B.Cu at (37.8, 5.25)
- added R67: R182,0603, Resistor_SMD:R_0603_1608Metric_Pad1.05x0.95mm_HandSolder, B.Cu at (41.8, 2.50)
- added R68: R104,0603, Resistor_SMD:R_0603_1608Metric_Pad1.05x0.95mm_HandSolder, F.Cu at (29.8, 74.8)
- added R69: R102,0603, Resistor_SMD:R_0603_1608Metric_Pad1.05x0.95mm_HandSolder, B.Cu at (33.0, 97.7)
- added R7: R102,0603, Resistor_SMD:R_0603_1608Metric_Pad1.05x0.95mm_HandSolder, B.Cu at (50.8, 70.8)
- added R70: R103,0603, Resistor_SMD:R_0603_1608Metric_Pad1.05x0.95mm_HandSolder, F.Cu at (29.8, 82.5)
- added R71: R104,0603, Resistor_SMD:R_0603_1608Metric_Pad1.05x0.95mm_HandSolder, F.Cu at (77.8, 78.6)
- added R72: R102,0603, Resistor_SMD:R_0603_1608Metric_Pad1.05x0.95mm_HandSolder, B.Cu at (78.2, 97.7)
- added R73: R103,0603, Resistor_SMD:R_0603_1608Metric_Pad1.05x0.95mm_HandSolder, F.Cu at (77.8, 82.5)
- added R74: R562,0603, Resistor_SMD:R_0603_1608Metric_Pad1.05x0.95mm_HandSolder, F.Cu at (59.5, 41.0)
- added R75: R103,0603, Resistor_SMD:R_0603_1608Metric_Pad1.05x0.95mm_HandSolder, F.Cu at (59.5, 37.5)
- added R76: R333,0603, Resistor_SMD:R_0603_1608Metric_Pad1.05x0.95mm_HandSolder, F.Cu at (59.5, 39.2)
- added R77: R562,0603, Resistor_SMD:R_0603_1608Metric_Pad1.05x0.95mm_HandSolder, F.Cu at (52.8, 30.0)
- added R78: R103,0603, Resistor_SMD:R_0603_1608Metric_Pad1.05x0.95mm_HandSolder, F.Cu at (52.2, 32.0)
- added R79: R333,0603, Resistor_SMD:R_0603_1608Metric_Pad1.05x0.95mm_HandSolder, F.Cu at (52.2, 33.8)
- added R8: R104,0603, Resistor_SMD:R_0603_1608Metric_Pad1.05x0.95mm_HandSolder, F.Cu at (93.5, 78.6)
- added R9: R102,0603, Resistor_SMD:R_0603_1608Metric_Pad1.05x0.95mm_HandSolder, B.Cu at (92.2, 97.7)
- added SW1: SW_Push, Button_Switch_SMD:SW_SPST_CK_RS282G05A3, F.Cu at (47.6, 68.0)
- added TH1: Thermistor_NTC, Resistor_SMD:R_0603_1608Metric_Pad1.05x0.95mm_HandSolder, F.Cu at (27.4, 21.6)
- added U1: orange_pi_zero, footprint-lib:orangepi-zero, B.Cu at (52.0, 69.5)
- added U10: A4988_MODULE, footprint-lib:Pololu_Breakout-16_15.2x20.3mm, F.Cu at (68.1, 74.4)
- added U11: MP2303A_ALT, footprint-lib:SOIC-8_3.9x4.9mm_P1.27mm,thermal_via, F.Cu at (68.0, 38.1)
- added U12: MP2303A_ALT, footprint-lib:SOIC-8_3.9x4.9mm_P1.27mm,thermal_via, F.Cu at (47.5, 35.1)
- added U2: A4988_MODULE, footprint-lib:Pololu_Breakout-16_15.2x20.3mm, F.Cu at (84.3, 74.4)
- added U4: A4988_MODULE, footprint-lib:Pololu_Breakout-16_15.2x20.3mm, F.Cu at (35.6, 74.4)
- added U5: A4988_MODULE, footprint-lib:Pololu_Breakout-16_15.2x20.3mm, F.Cu at (3.18, 74.4)
- added U6: A4988_MODULE, footprint-lib:Pololu_Breakout-16_15.2x20.3mm, F.Cu at (25.0, 57.9)
- added U7: A4988_MODULE, footprint-lib:Pololu_Breakout-16_15.2x20.3mm, F.Cu at (25.0, 41.9)
- added U8: STM32F407VET6, w_smd_lqfp:TQFP-100, F.Cu at (40.9, 57.5)
- added U9: A4988_MODULE, footprint-lib:Pololu_Breakout-16_15.2x20.3mm, F.Cu at (19.4, 74.4)
- added Y1: O_8M, Crystal:Crystal_HC49-4H_Vertical, F.Cu at (30.6, 64.0)
- moved C4 87.0 mm to (58.1, 90.2)
- moved U3 86.5 mm to (51.9, 74.4)
- moved D3 86.2 mm to (63.1, 97.7)
- moved J4 86.2 mm to (55.1, 77.0)
- moved R12 86.1 mm to (63.1, 97.7)
- moved R13 86.1 mm to (61.5, 74.8)
- moved J5 86.0 mm to (56.8, 97.3), turned to 180 degrees
- moved R11 86.0 mm to (61.5, 78.6)
- moved C5 85.9 mm to (61.5, 82.5)
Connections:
- net +3V3_STM32 renamed +3V3
- net /Z_DIR renamed /Z_~E1_STEP~PER_DRIVER/Z_DIR
- net /Z_STEP renamed /Z_~E1_STEP~PER_DRIVER/Z_STEP
- net /~Z_EN~ renamed /Z_~E1_STEP~PER_DRIVER/~Z_EN~
- U3 pad 11: Net-(J5-Pad4) -> Net-(J5-Pad1)
- U3 pad 12: Net-(J5-Pad3) -> Net-(J5-Pad2)
- U3 pad 13: Net-(J5-Pad2) -> Net-(J5-Pad3)
- U3 pad 14: Net-(J5-Pad1) -> Net-(J5-Pad4)
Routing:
- net /Z_~E1_STEP~PER_DRIVER/~Z_EN~: track 34.7 -> 0.00 mm
- net +12V: track 32.7 -> 0.00 mm
- net GND: track 27.9 -> 0.00 mm
- net +3V3: track 27.8 -> 0.00 mm
- net Net-(J5-Pad1): track 21.5 -> 0.00 mm
- net Net-(J5-Pad2): track 18.0 -> 0.00 mm
- net Net-(J5-Pad3): track 14.7 -> 0.00 mm
- net Net-(J5-Pad4): track 11.4 -> 0.00 mm
- net Net-(J4-Pad1): track 11.3 -> 0.00 mm
- net Net-(J4-Pad3): track 3.86 -> 0.00 mm
- net Net-(J4-Pad5): track 3.86 -> 0.00 mm
- net Net-(U3-Pad5): track 2.54 -> 0.00 mm
- net Net-(D3-Pad2): track 2.25 -> 0.00 mm, vias 1 -> 0
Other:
- board outline added: 100 x 100 mm
